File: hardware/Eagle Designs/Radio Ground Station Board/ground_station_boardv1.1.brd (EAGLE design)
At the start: 3 parts, among them J1 MCX-J-P-H-RA-TH1, U1 RFM23BP

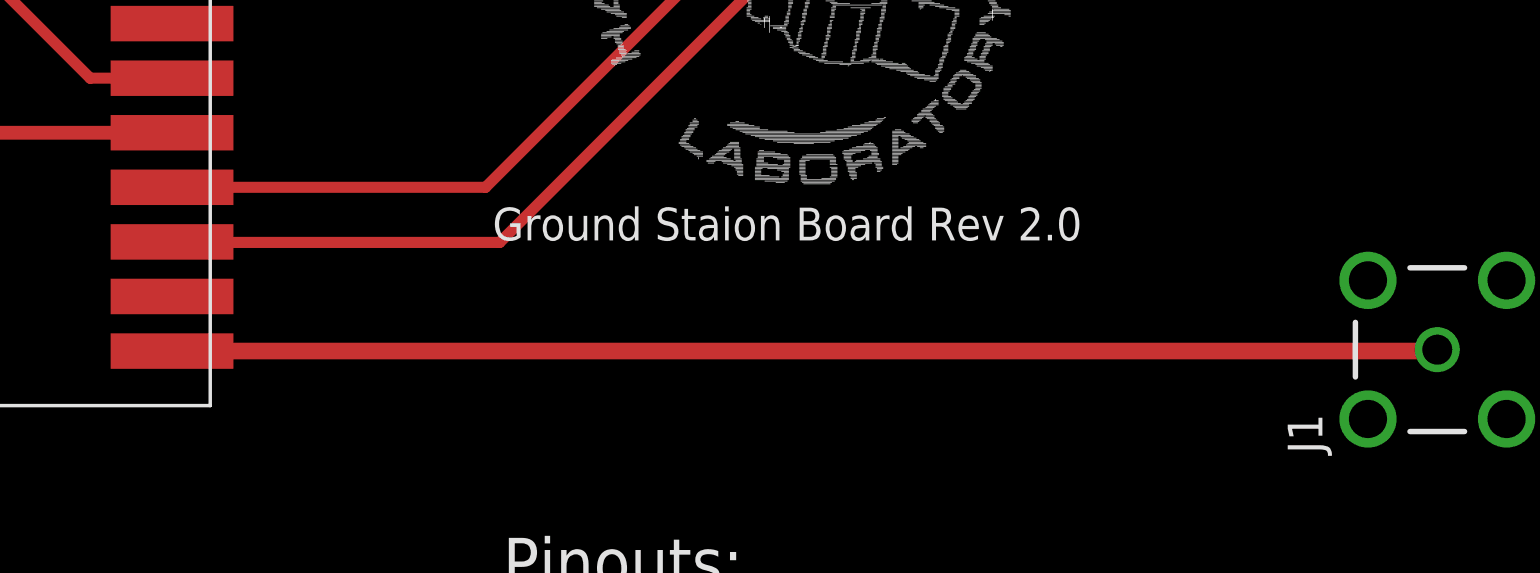
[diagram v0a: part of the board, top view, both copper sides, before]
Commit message: Added RF ground plane to ground station board.
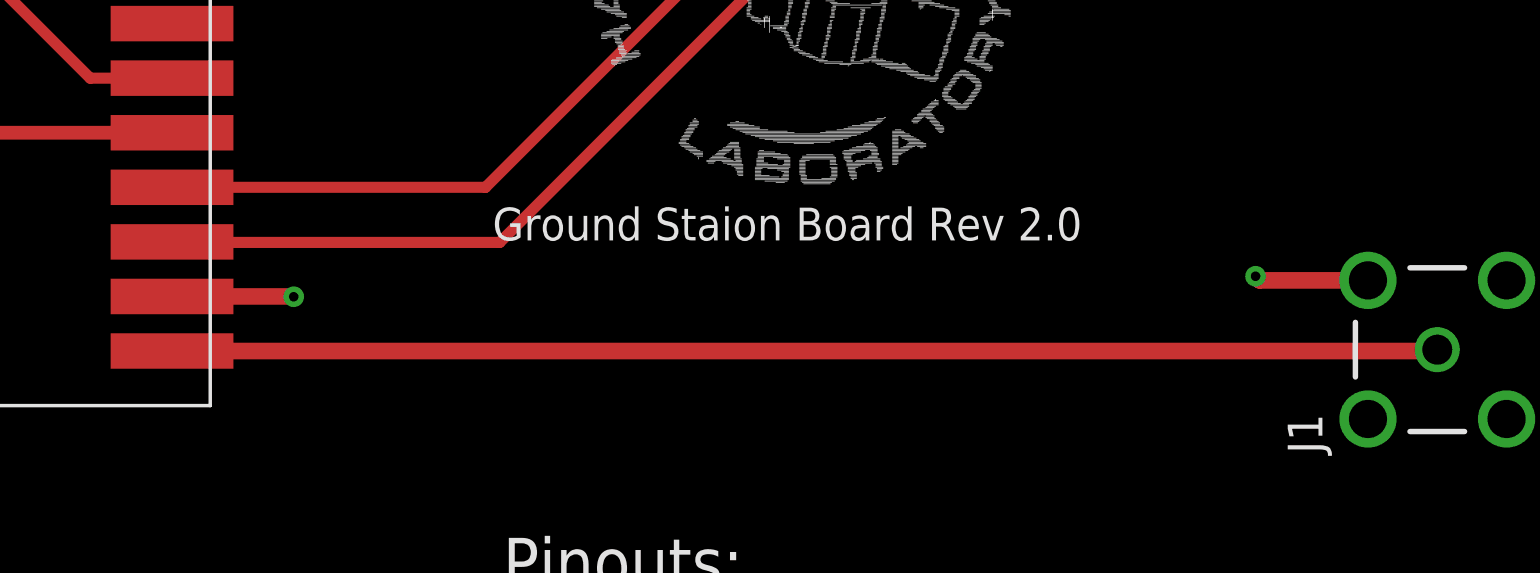
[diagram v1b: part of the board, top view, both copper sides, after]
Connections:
- removed net ANT_GND: U1.10
- new net RF_GND: J1.S1, J1.S2, J1.S3, J1.S4, U1.10
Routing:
- net RF_GND: track 0.00 -> 8.65 mm, vias 0 -> 2
- added copper zone on layer 15, net RF_GND
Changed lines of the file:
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@@
 <setting verticaltext="up"/>
 </settings>
-<grid distance="0.01" unitdist="mm" unit="mm" style="lines" multiple="1" display="yes" altdistance="0.025" altunitdist="mm" altunit="mm"/>
+<grid distance="0.25" unitdist="mm" unit="mm" style="lines" multiple="1" display="yes" altdistance="0.025" altunitdist="mm" altunit="mm"/>
 <layers>
 <layer number="1" name="Top" color="4" fill="1" visible="yes" active="yes"/>
@@
 </layers>
 <board>
-<fusionsync huburn="a.YnVzaW5lc3M6aGF3YWlpMzk3" projecturn="a.YnVzaW5lc3M6aGF3YWlpMzk3I0QyMDIxMDIxMTM4MTc0NzIyNg" f3durn="urn:adsk.wipprod:dm.lineage:WPvLawa_Q36ULf1lFy3S-g" pcbguid="" lastpulledtime="" lastsyncedchangeguid="" latestrevisionid="935d8412-0a8b-471e-9db4-d59a038692ee" lastsyncedrevisionid="935d8412-0a8b-471e-9db4-d59a038692ee" lastboardhashguid="5ede64c8-f60e-0077-9b9e-ecb65980b17f" lastpushedtime="2021-09-29T01:22:19Z" linktopcb3d="false"/>
+<fusionsync huburn="a.YnVzaW5lc3M6aGF3YWlpMzk3" projecturn="a.YnVzaW5lc3M6aGF3YWlpMzk3I0QyMDIxMDIxMTM4MTc0NzIyNg" f3durn="urn:adsk.wipprod:dm.lineage:WPvLawa_Q36ULf1lFy3S-g" pcbguid="" lastpulledtime="" lastsyncedchangeguid="" latestrevisionid="935d8412-0a8b-471e-9db4-d59a038692ee" lastsyncedrevisionid="935d8412-0a8b-471e-9db4-d59a038692ee" lastboardhashguid="5ede64c8-f60e-0077-9b9e-ecb65980b17f" lastpushedtime="2021-09-29T01:22:19Z" linktopcb3d="true"/>
 <plain>
 <text x="49.0388" y="41.564" size="1.2" layer="25" font="vector">Ground Staion Board Rev 2.0</text>
@@
 <wire x1="57.93" y1="85.72" x2="64.3" y2="79.35" width="0.4064" layer="1"/>
 </signal>
-<signal name="ANT_GND">
-<contactref element="U1" pad="10"/>
-</signal>
 <signal name="GND">
 <contactref element="U1" pad="8"/>
@@
 <vertex x="93.4" y="-5.8"/>
 </polygon>
-<polygon width="0.3048" layer="15" grouprefs="IMU">
+<polygon width="0.3048" layer="15" rank="2" grouprefs="IMU">
 <vertex x="91.4" y="97"/>
 <vertex x="-3.8" y="97"/>
@@
 <wire x1="37.29" y1="37.51" x2="83.61" y2="37.51" width="0.6096" layer="1"/>
 </signal>
+<signal name="RF_GND">
+<polygon width="0.1524" layer="15">
+<vertex x="90" y="48"/>
+<vertex x="33.25" y="48"/>
+<vertex x="33.25" y="24.25"/>
+<vertex x="90" y="24.25"/>
+</polygon>
+<contactref element="J1" pad="S3"/>
+<contactref element="J1" pad="S4"/>
+<contactref element="J1" pad="S1"/>
+<contactref element="J1" pad="S2"/>
+<contactref element="U1" pad="10"/>
+<via x="41.75" y="39.5" extent="1-16" drill="0.35"/>
+<via x="77" y="40.25" extent="1-16" drill="0.35"/>
+<wire x1="37.29" y1="39.51" x2="41.74" y2="39.51" width="0.6096" layer="1"/>
+<wire x1="41.74" y1="39.51" x2="41.75" y2="39.5" width="0.6096" layer="1"/>
+<wire x1="81.12" y1="40.1" x2="77.15" y2="40.1" width="0.6096" layer="1"/>
+<wire x1="77.15" y1="40.1" x2="77" y2="40.25" width="0.6096" layer="1"/>
+</signal>
 </signals>

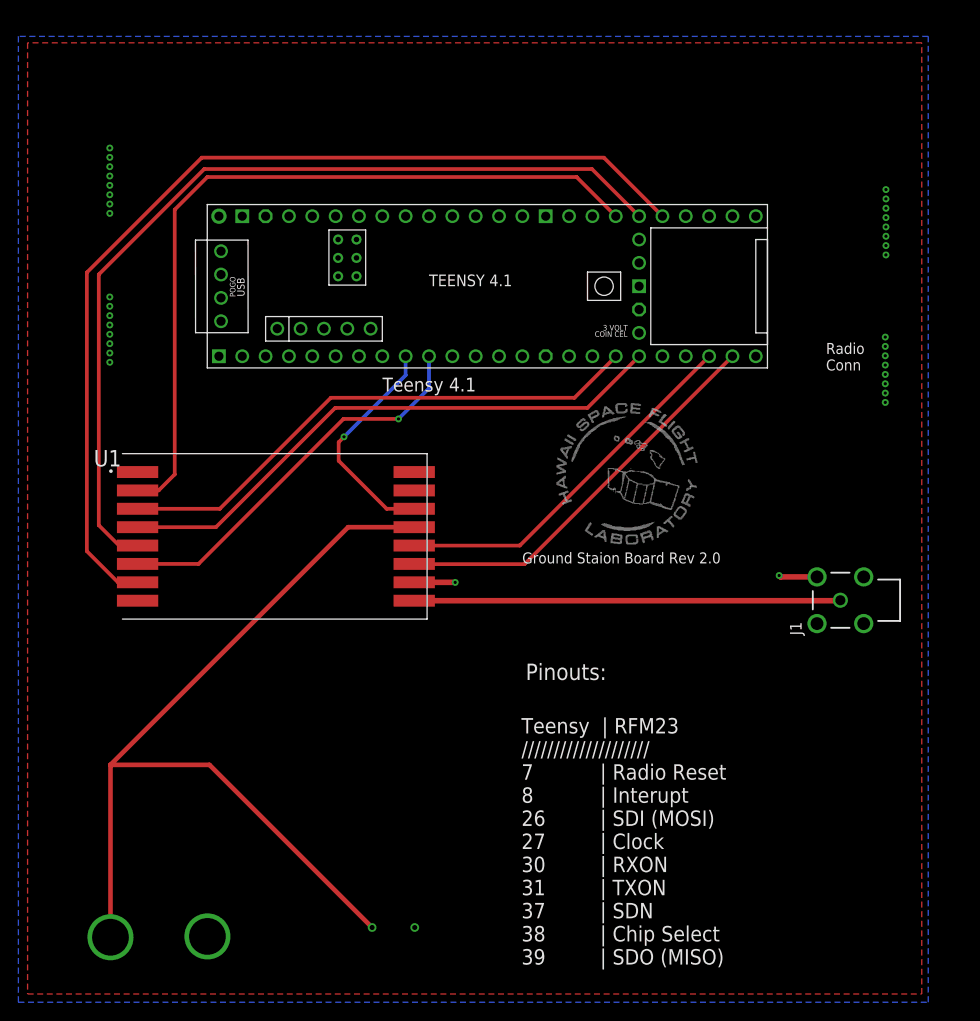
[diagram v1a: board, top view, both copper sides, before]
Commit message: Modified pin configuration on the ground station board to match OBC 4.24.
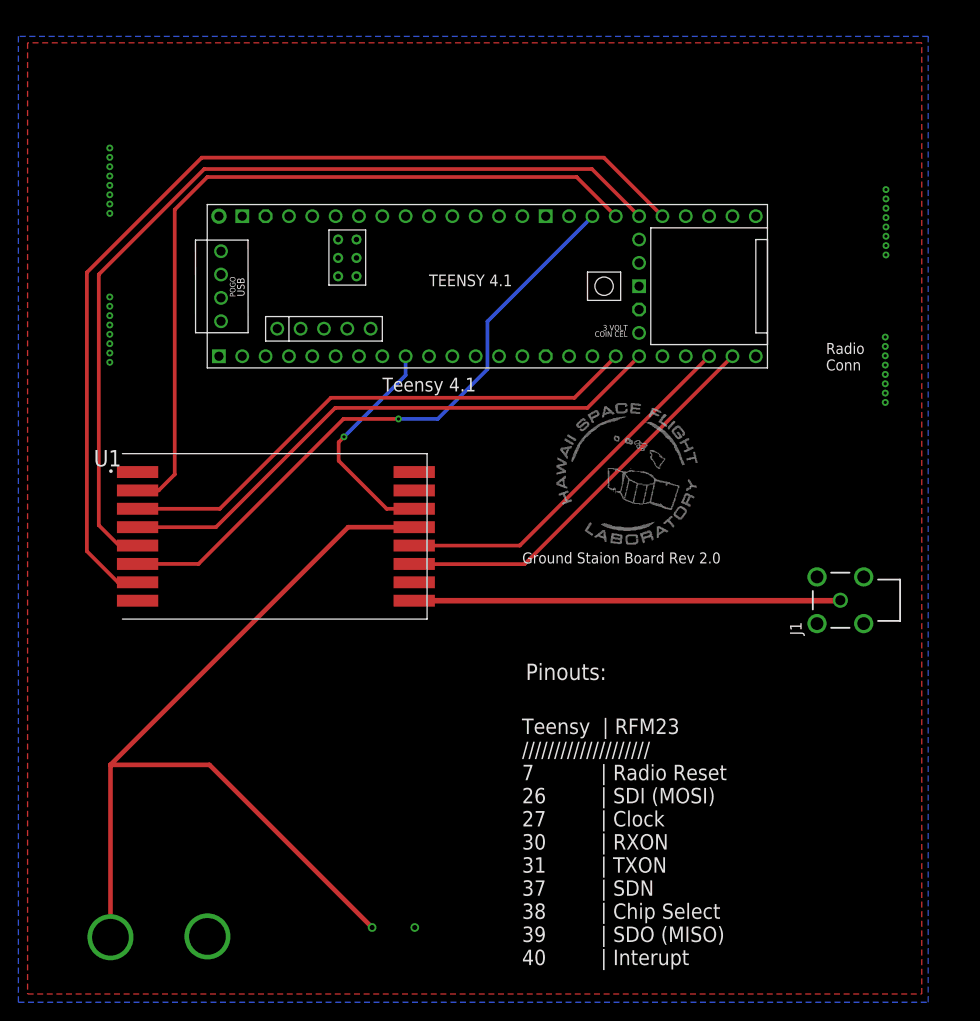
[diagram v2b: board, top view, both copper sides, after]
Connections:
- removed net RF_GND: J1.S1, J1.S2, J1.S3, J1.S4, U1.10
- new net ANT_GND: U1.10
- net NIRQ: now also U$1.40-A16/CS1; no longer U$1.8-TX2/IN1
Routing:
- net NIRQ: track 43.1 -> 68.2 mm
- net RF_GND: track 8.65 -> 0.00 mm, vias 2 -> 0
- removed copper zone on layer 15, net RF_GND
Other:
- board text added: "Teensy | RFM23 //////////////////// 7 | Radio Reset 26 | SDI (MOSI) 27 | Clock 30 | RXON 31 | TXON 37 | SDN 38 | Chip Select 39 | SDO (MISO) 40 | Interupt"
- board text removed: "Teensy | RFM23 //////////////////// 7 | Radio Reset 8 | Interupt 26 | SDI (MOSI) 27 | Clock 30 | RXON 31 | TXON 37 | SDN 38 | Chip Select 39 | SDO (MISO)"
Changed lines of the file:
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@@
 <setting verticaltext="up"/>
 </settings>
-<grid distance="0.25" unitdist="mm" unit="mm" style="lines" multiple="1" display="yes" altdistance="0.025" altunitdist="mm" altunit="mm"/>
+<grid distance="0.01" unitdist="mm" unit="mm" style="lines" multiple="1" display="yes" altdistance="0.025" altunitdist="mm" altunit="mm"/>
 <layers>
 <layer number="1" name="Top" color="4" fill="1" visible="yes" active="yes"/>
@@
 </layers>
 <board>
-<fusionsync huburn="a.YnVzaW5lc3M6aGF3YWlpMzk3" projecturn="a.YnVzaW5lc3M6aGF3YWlpMzk3I0QyMDIxMDIxMTM4MTc0NzIyNg" f3durn="urn:adsk.wipprod:dm.lineage:WPvLawa_Q36ULf1lFy3S-g" pcbguid="" lastpulledtime="" lastsyncedchangeguid="" latestrevisionid="935d8412-0a8b-471e-9db4-d59a038692ee" lastsyncedrevisionid="935d8412-0a8b-471e-9db4-d59a038692ee" lastboardhashguid="5ede64c8-f60e-0077-9b9e-ecb65980b17f" lastpushedtime="2021-09-29T01:22:19Z" linktopcb3d="true"/>
+<fusionsync huburn="a.YnVzaW5lc3M6aGF3YWlpMzk3" projecturn="a.YnVzaW5lc3M6aGF3YWlpMzk3I0QyMDIxMDIxMTM4MTc0NzIyNg" f3durn="urn:adsk.wipprod:dm.lineage:WPvLawa_Q36ULf1lFy3S-g" pcbguid="" lastpulledtime="" lastsyncedchangeguid="" latestrevisionid="935d8412-0a8b-471e-9db4-d59a038692ee" lastsyncedrevisionid="935d8412-0a8b-471e-9db4-d59a038692ee" lastboardhashguid="5ede64c8-f60e-0077-9b9e-ecb65980b17f" lastpushedtime="2021-09-29T01:22:19Z" linktopcb3d="false"/>
 <plain>
 <text x="49.0388" y="41.564" size="1.2" layer="25" font="vector">Ground Staion Board Rev 2.0</text>
@@
 Conn</text>
 <text x="49.4188" y="28.884" size="1.778" layer="25" font="vector">Pinouts:</text>
-<text x="48.9588" y="-4.596" size="1.6764" layer="25" font="vector">Teensy  | RFM23
+<text x="49.0188" y="-4.656" size="1.6764" layer="25" font="vector">Teensy  | RFM23
 ////////////////////
 7           | Radio Reset
-8           | Interupt
 26         | SDI (MOSI)
 27         | Clock
@@
 38         | Chip Select
 39         | SDO (MISO)
+40         | Interupt
 </text>
 </plain>
@@
 </signal>
 <signal name="NIRQ">
-<contactref element="U$1" pad="8-TX2/IN1"/>
 <contactref element="U1" pad="6"/>
 <via x="35.58" y="57.29" extent="1-16" drill="0.35"/>
@@
 <wire x1="29.6" y1="57.29" x2="13.82" y2="41.51" width="0.4064" layer="1"/>
 <wire x1="29.6" y1="57.29" x2="35.58" y2="57.29" width="0.4064" layer="1"/>
-<wire x1="35.58" y1="57.29" x2="38.9" y2="60.61" width="0.4064" layer="16"/>
-<wire x1="38.9" y1="60.61" x2="38.9" y2="64.11" width="0.4064" layer="16"/>
+<contactref element="U$1" pad="40-A16/CS1"/>
+<wire x1="35.58" y1="57.29" x2="39.84" y2="57.29" width="0.4064" layer="16"/>
+<wire x1="45.26" y1="67.9" x2="56.68" y2="79.32" width="0.4064" layer="16"/>
+<wire x1="39.84" y1="57.29" x2="45.26" y2="62.71" width="0.4064" layer="16"/>
+<wire x1="45.26" y1="62.71" x2="45.26" y2="67.9" width="0.4064" layer="16"/>
+<wire x1="56.68" y1="79.32" x2="56.68" y2="79.35" width="0" layer="19" extent="16-16"/>
 </signal>
 <signal name="RX_ON">
@@
 <wire x1="57.93" y1="85.72" x2="64.3" y2="79.35" width="0.4064" layer="1"/>
 </signal>
+<signal name="ANT_GND">
+<contactref element="U1" pad="10"/>
+</signal>
 <signal name="GND">
 <contactref element="U1" pad="8"/>
@@
 <vertex x="93.4" y="-5.8"/>
 </polygon>
-<polygon width="0.3048" layer="15" rank="2" grouprefs="IMU">
+<polygon width="0.3048" layer="15" grouprefs="IMU">
 <vertex x="91.4" y="97"/>
 <vertex x="-3.8" y="97"/>
@@
 <wire x1="37.29" y1="37.51" x2="83.61" y2="37.51" width="0.6096" layer="1"/>
 </signal>
-<signal name="RF_GND">
-<polygon width="0.1524" layer="15">
-<vertex x="90" y="48"/>
-<vertex x="33.25" y="48"/>
-<vertex x="33.25" y="24.25"/>
-<vertex x="90" y="24.25"/>
-</polygon>
-<contactref element="J1" pad="S3"/>
-<contactref element="J1" pad="S4"/>
-<contactref element="J1" pad="S1"/>
-<contactref element="J1" pad="S2"/>
-<contactref element="U1" pad="10"/>
-<via x="41.75" y="39.5" extent="1-16" drill="0.35"/>
-<via x="77" y="40.25" extent="1-16" drill="0.35"/>
-<wire x1="37.29" y1="39.51" x2="41.74" y2="39.51" width="0.6096" layer="1"/>
-<wire x1="41.74" y1="39.51" x2="41.75" y2="39.5" width="0.6096" layer="1"/>
-<wire x1="81.12" y1="40.1" x2="77.15" y2="40.1" width="0.6096" layer="1"/>
-<wire x1="77.15" y1="40.1" x2="77" y2="40.25" width="0.6096" layer="1"/>
-</signal>
 </signals>

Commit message: Fixed RF ground station board... again.
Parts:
- moved J1 4.14 mm to (85.9, 41.0)
- moved U1 4.14 mm to (24.0, 48.0)
- moved U$1 4.14 mm to (48.8, 75.2)
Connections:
- removed net ANT_GND: U1.10
- new net RF_GND: J1.S1, J1.S2, J1.S3, J1.S4, U1.10
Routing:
- net RF_GND: track 0.00 -> 5.47 mm, vias 0 -> 1
- added copper zone on layer 15, net RF_GND
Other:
- board outline added: 95 x 97 mm
- board text added: "+"
- board text added: "-"
- board text added: "Ground Staion Board Rev 3.0"
- board text removed: "Ground Staion Board Rev 2.0"
